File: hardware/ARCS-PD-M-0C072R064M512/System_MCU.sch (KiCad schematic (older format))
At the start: 47 parts

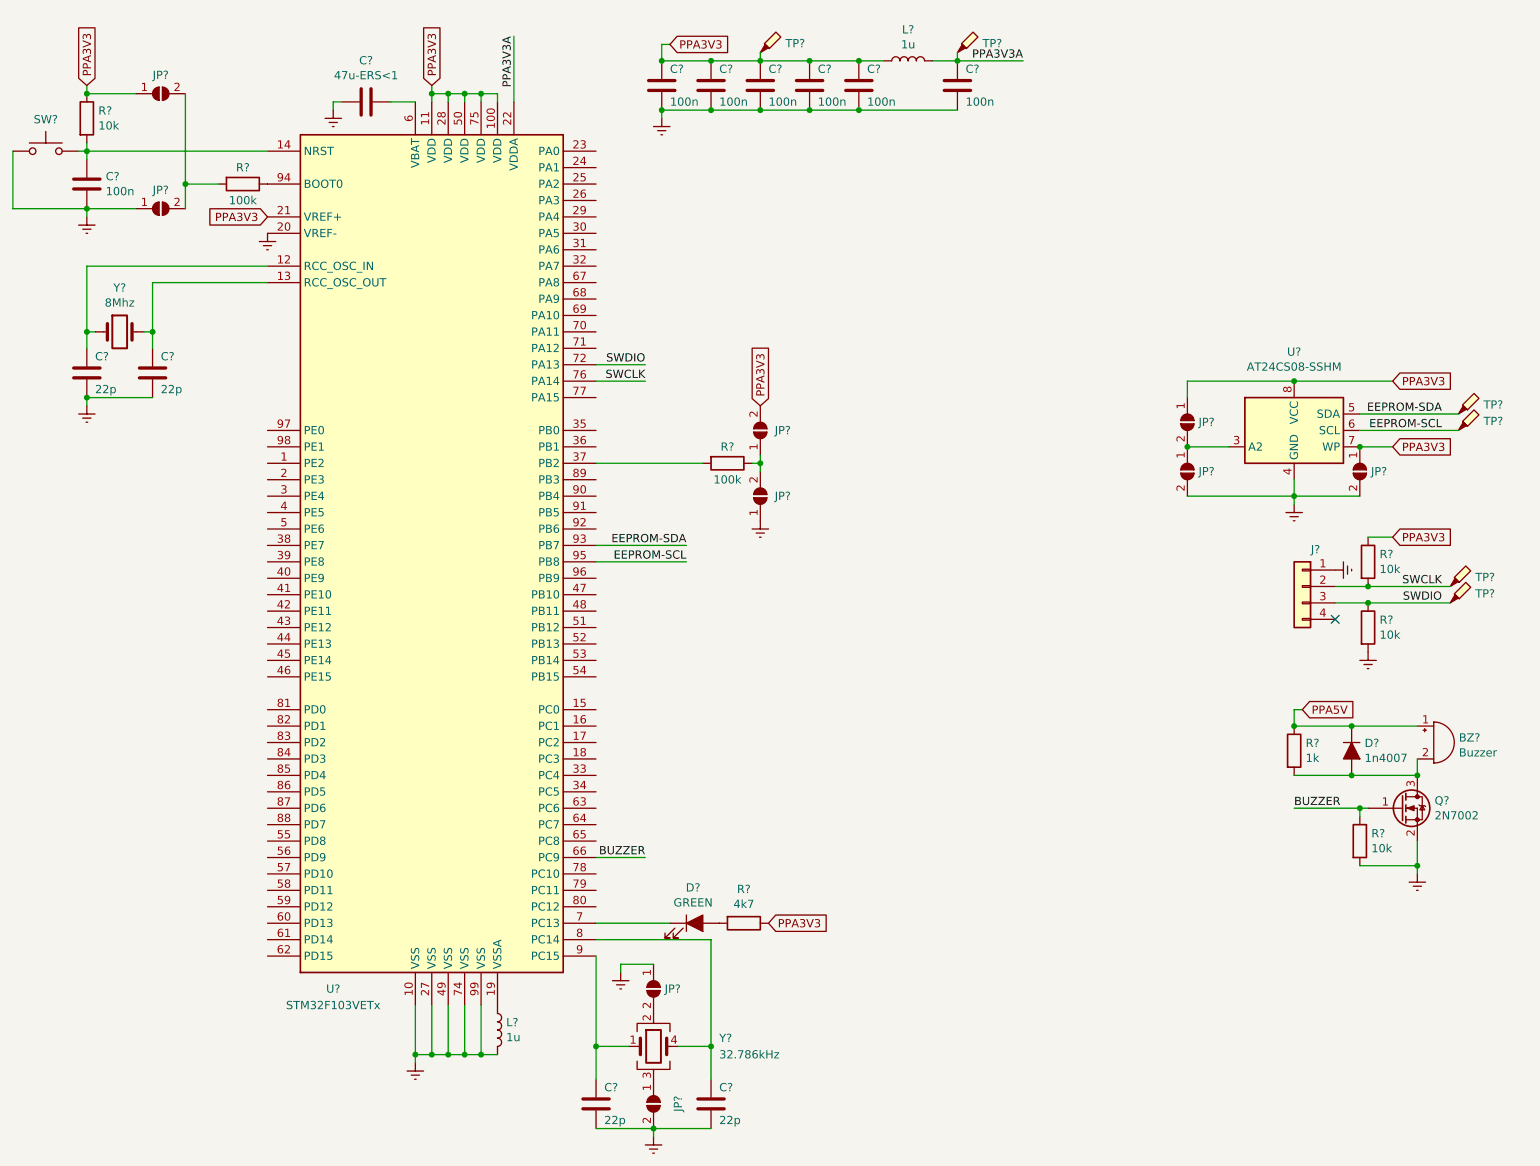
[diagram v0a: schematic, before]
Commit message: Create cards for input and output interface.
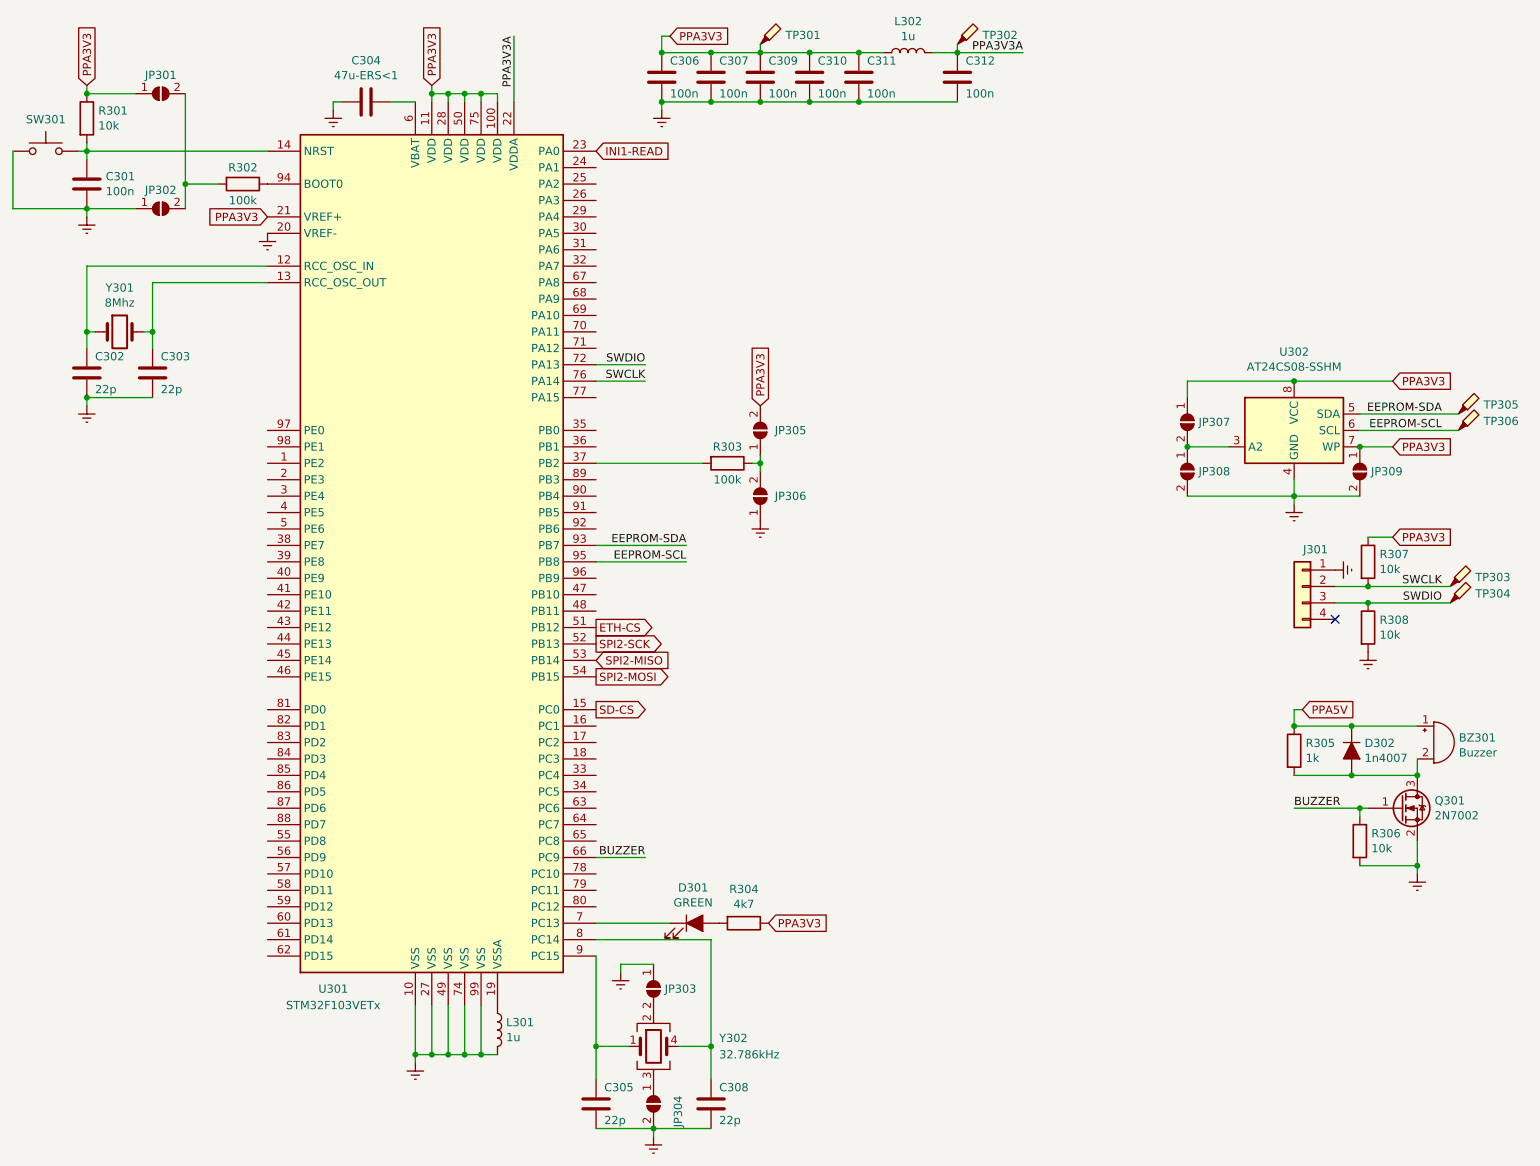
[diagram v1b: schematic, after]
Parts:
- gave numbers to parts that had none: 47
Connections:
- net SD-CS: now reaches U301.15 (PC0)
- net INI1-READ: now reaches U301.23 (PA0)
- net ETH-CS: now reaches U301.51 (PB12)
- net SPI2-SCK: now reaches U301.52 (PB13)
- net SPI2-MISO: now reaches U301.53 (PB14)
- net SPI2-MOSI: now reaches U301.54 (PB15)
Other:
- moved on the sheet: C306, C307, C309, C310, C311, C312, L302, TP301, TP302
